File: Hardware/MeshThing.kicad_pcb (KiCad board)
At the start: 4 copper layers, 19.1 x 24.7 mm, 24 parts, among them IC1 ATMEGA2564/1284/644RFR2, P1 CONN34

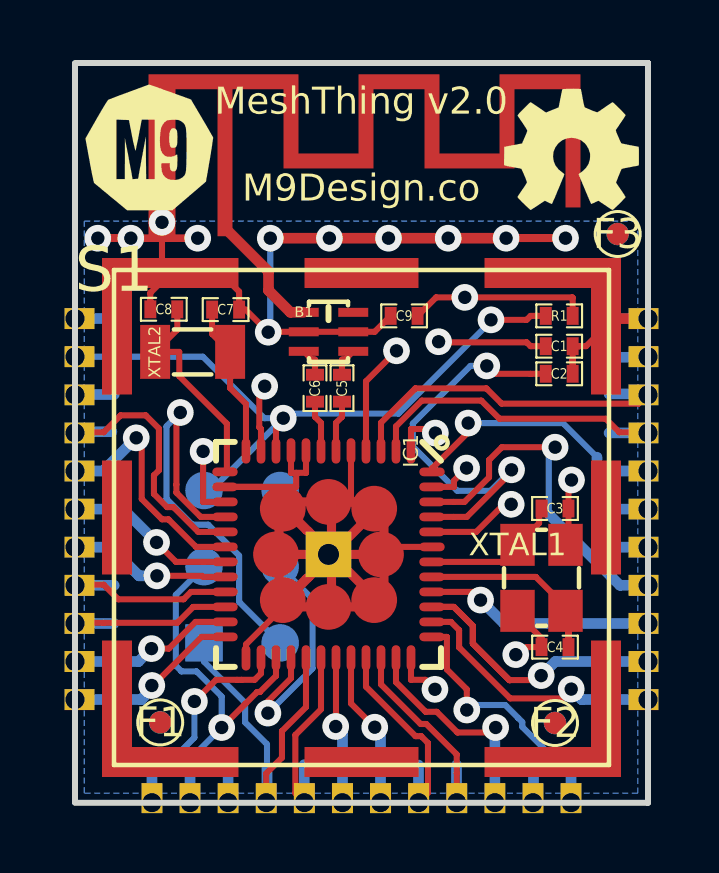
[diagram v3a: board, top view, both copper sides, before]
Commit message: Minor changes, initial positions file for MT.
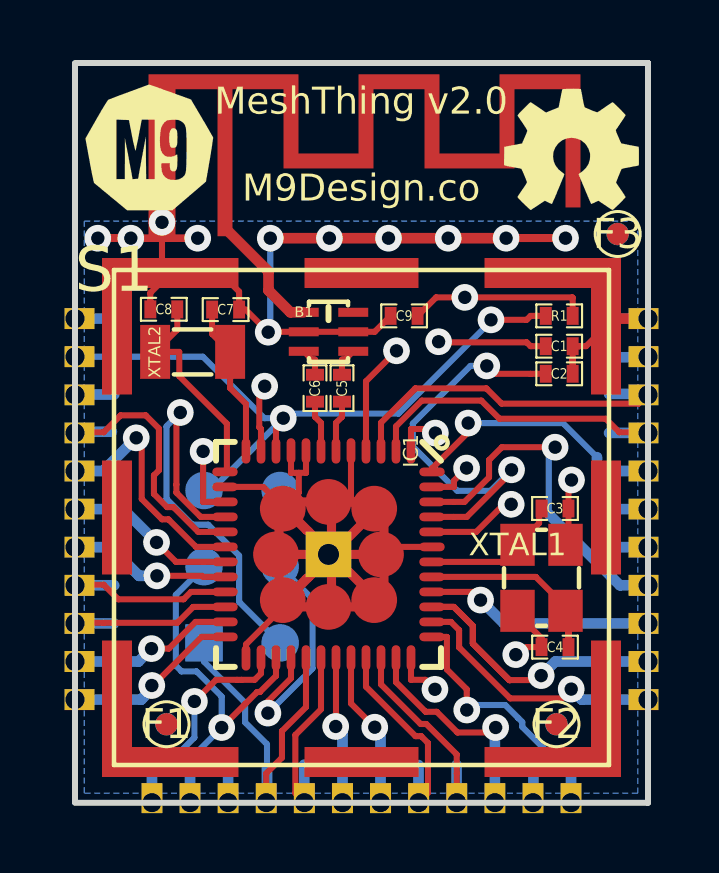
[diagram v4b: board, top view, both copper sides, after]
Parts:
- moved F1 0.22 mm to (143.5, 109.7)
- moved F2 0.06 mm to (156.5, 109.7)
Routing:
- net GND: track 96.3 -> 94.6 mm
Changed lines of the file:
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@@
   )
   (layers
-    (15 F.Cu signal hide)
+    (15 F.Cu signal)
     (2 Inner2.Cu power hide)
     (1 Inner1.Cu signal hide)
@@
     (18 B.Paste user hide)
     (19 F.Paste user hide)
-    (20 B.SilkS user)
+    (20 B.SilkS user hide)
     (21 F.SilkS user hide)
     (22 B.Mask user)
@@
     (aux_axis_origin 150 100)
     (grid_origin 150 100)
-    (visible_elements FFFFCE5B)
+    (visible_elements FFFFCA3B)
     (pcbplotparams
       (layerselection 284983303)
@@
   )
   (module _MT_MC_Pretty:_MT_Fiducial (layer F.Cu)
-    (at 156.45 109.67)
+    (at 156.5 109.71)
+    (attr smd)
     (fp_text reference F2 (at 0 0) (layer F.SilkS)
       (effects (font (size 1 1) (thickness 0.15)))
@@
   )
   (module _MT_MC_Pretty:_MT_Fiducial (layer F.Cu)
-    (at 143.29 109.65)
+    (at 143.5 109.71)
+    (attr smd)
     (fp_text reference F1 (at 0 0) (layer F.SilkS)
       (effects (font (size 1 1) (thickness 0.15)))
@@
   (module _MT_MC_Pretty:16MHz-3.2x2.5mm-TSX-3225 (layer F.Cu)
     (at 156 104.83)
+    (attr smd)
     (fp_text reference XTAL1 (at -0.8 -1.1) (layer F.SilkS)
       (effects (font (size 0.75 0.75) (thickness 0.15)))
@@
   (module _MT_MC_Pretty:_MT_MC_EMIShield-16.5x16.5 (layer F.Cu)
     (at 150 102.82)
+    (attr smd)
     (fp_text reference S1 (at -8.25 -8.25) (layer F.SilkS)
       (effects (font (size 1.5 1.5) (thickness 0.15)))
@@
   (module _MT_MC_Pretty:_MC_TF32D-32768-Crystal (layer F.Cu)
     (at 144.37 97.3)
+    (attr smd)
     (fp_text reference XTAL2 (at -1.26 0 90) (layer F.SilkS)
       (effects (font (size 0.4 0.4) (thickness 0.1)))
@@
   (module _MT_MC_Pretty:_MT_Fiducial (layer F.Cu)
     (at 158.54 93.37)
+    (attr smd)
     (fp_text reference F3 (at 0 0) (layer F.SilkS)
       (effects (font (size 1 1) (thickness 0.15)))
@@
   (segment (start 153.3706 95.41) (end 150.2596 95.41) (width 0.2032) (layer Inner1.Cu) (net 1))
   (segment (start 153.4432 95.4826) (end 153.3706 95.41) (width 0.2032) (layer Inner1.Cu) (net 1))
+  (segment (start 147.91 101.3313) (end 147.91 101.992) (width 0.2032) (layer F.Cu) (net 2))
+  (segment (start 147.91 101.992) (end 147.376 102.526) (width 0.2032) (layer F.Cu) (net 2))
+  (segment (start 147.376 102.526) (end 147.376 102.456) (width 0.2032) (layer F.Cu) (net 2))
+  (segment (start 145.45068 101.8) (end 146.72 101.8) (width 0.2032) (layer F.Cu) (net 2))
+  (segment (start 147.376 102.456) (end 146.72 101.8) (width 0.2032) (layer F.Cu) (net 2))
   (segment (start 150.97042 96.1) (end 150.44042 96.63) (width 0.2032) (layer F.Cu) (net 2))
   (segment (start 150.44042 96.63) (end 149.725 96.63) (width 0.2032) (layer F.Cu) (net 2))
@@
   (segment (start 143.35 93.51) (end 144.54 93.51) (width 0.254) (layer F.Cu) (net 2))
   (via (at 144.54 93.51) (size 0.889) (layers F.Cu B.Cu) (net 2))
-  (segment (start 145.45068 101.8) (end 147.11 101.8) (width 0.2032) (layer F.Cu) (net 2))
-  (segment (start 147.376 102.066) (end 147.376 102.526) (width 0.2032) (layer F.Cu) (net 2))
-  (segment (start 147.11 101.8) (end 147.376 102.066) (width 0.2032) (layer F.Cu) (net 2))
   (segment (start 159.525 96.19) (end 158.26 96.19) (width 0.3556) (layer B.Cu) (net 2))
   (segment (start 145.91958 95.89) (end 146.1378 95.89) (width 0.2032) (layer F.Cu) (net 2))
@@
   (segment (start 148.9 102.3) (end 148.5409 102.3) (width 0.3048) (layer F.Cu) (net 2))
   (segment (start 148.5409 102.3) (end 147.702 102.3) (width 0.3048) (layer F.Cu) (net 2))
-  (segment (start 145.4507 101.8) (end 146.1813 101.8) (width 0.2032) (layer F.Cu) (net 2))
   (segment (start 147.702 105.8) (end 148.9 105.8) (width 0.3048) (layer F.Cu) (net 2))
   (segment (start 146.15 107.05) (end 146.15 107.4993) (width 0.2032) (layer F.Cu) (net 2))
@@
   (segment (start 148.15 100.6007) (end 148.15 101.3313) (width 0.2032) (layer F.Cu) (net 2))
   (segment (start 147.65 100.6007) (end 147.65 101.3313) (width 0.2032) (layer F.Cu) (net 2))
-  (segment (start 148.15 101.3313) (end 147.8219 101.3313) (width 0.2032) (layer F.Cu) (net 2))
+  (segment (start 148.15 101.3313) (end 147.91 101.3313) (width 0.2032) (layer F.Cu) (net 2))
+  (segment (start 147.91 101.3313) (end 147.8219 101.3313) (width 0.2032) (layer F.Cu) (net 2))
   (segment (start 147.8219 101.3313) (end 147.65 101.3313) (width 0.2032) (layer F.Cu) (net 2))
-  (segment (start 147.8219 101.8) (end 146.1813 101.8) (width 0.2032) (layer F.Cu) (net 2))
-  (segment (start 147.8219 101.8) (end 147.8219 101.3313) (width 0.2032) (layer F.Cu) (net 2))
   (segment (start 149.65 102.3) (end 149.65 100.6007) (width 0.2032) (layer F.Cu) (net 2))
   (segment (start 150.298 102.3) (end 149.65 102.3) (width 0.3048) (layer F.Cu) (net 2))

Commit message: Removed ICSP pads.
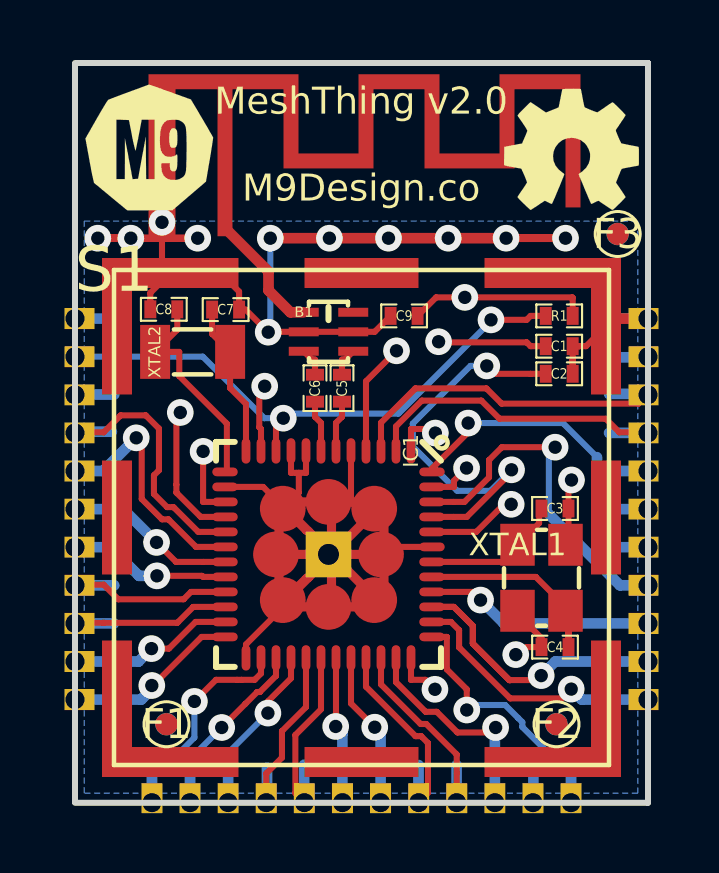
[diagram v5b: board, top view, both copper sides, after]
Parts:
- removed H1: ICSP, _MT_MC_Pretty:_MC_pin_pad_3x2
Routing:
- net +3.3V: track 61.1 -> 51.3 mm
- net SCK: track 15.1 -> 8.41 mm
- net MOSI: track 14.6 -> 8.65 mm
- net MISO: track 11.6 -> 6.53 mm
- net Reset: track 22.9 -> 19.3 mm
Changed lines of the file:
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@@
 (kicad_pcb (version 3) (host pcbnew "(2013-12-14 BZR 4555)-product")
   (general
-    (links 85)
+    (links 79)
     (no_connects 0)
     (area 140.349999 87.569999 159.650001 112.430001)
     (thickness 1.6)
     (drawings 8)
-    (tracks 588)
+    (tracks 565)
     (zones 0)
-    (modules 24)
+    (modules 23)
     (nets 47)
   )
@@
     (aux_axis_origin 150 100)
     (grid_origin 150 100)
-    (visible_elements FFFFCA3B)
+    (visible_elements FFFF4E3B)
     (pcbplotparams
       (layerselection 284983303)
@@
       (xy 1.46558 -0.05842) (xy 1.56718 -0.06858) (xy 1.57988 -0.05842) (xy 1.57988 -0.05842)) (layer B.SilkS) (width 0.00254))
   )
-  (module _MT_MC_Pretty:_MC_pin_pad_3x2 (layer B.Cu)
-    (at 146.02 104.46 90)
-    (descr "Double rangee de contacts 2 x 4 pins")
-    (tags CONN)
-    (fp_text reference H1 (at 0 3.81 90) (layer B.SilkS) hide
-      (effects (font (size 1.016 1.016) (thickness 0.2032)) (justify mirror))
-    )
-    (fp_text value ICSP (at 0 -3.81 90) (layer B.SilkS) hide
-      (effects (font (size 1.016 1.016) (thickness 0.2032)) (justify mirror))
-    )
-    (fp_text user ICSP (at -4.6 0 360) (layer B.SilkS)
-      (effects (font (size 0.5 0.5) (thickness 0.125)) (justify mirror))
-    )
-    (fp_line (start -3.81 2.52) (end -3.81 -1.74) (layer B.SilkS) (width 0.2032))
-    (fp_line (start 3.81 -2.54) (end -3 -2.55) (layer B.SilkS) (width 0.2032))
-    (fp_line (start -3.01 -2.54) (end -3.81 -1.74) (layer B.SilkS) (width 0.2032))
-    (fp_circle (center -3.79 -2.474) (end -4.04 -2.474) (layer B.SilkS) (width 0.254))
-    (fp_line (start -3.81 2.54) (end 3.81 2.54) (layer B.SilkS) (width 0.2032))
-    (fp_line (start 3.81 2.54) (end 3.81 -2.54) (layer B.SilkS) (width 0.2032))
-    (pad 1 smd rect (at -2.54 -1.27 90) (size 1.25 1.25) (layers B.Cu B.Mask)
-      (net 3 MISO))
-    (pad 2 smd circle (at -2.54 1.27 90) (size 1.25 1.25) (layers B.Cu B.Mask)
-      (net 1 +3.3V))
-    (pad 3 smd circle (at 0 -1.27 90) (size 1.25 1.25) (layers B.Cu B.Mask)
-      (net 42 SCK))
-    (pad 4 smd circle (at 0 1.27 90) (size 1.25 1.25) (layers B.Cu B.Mask)
-      (net 4 MOSI))
-    (pad 5 smd circle (at 2.54 -1.27 90) (size 1.25 1.25) (layers B.Cu B.Mask)
-      (net 41 Reset))
-    (pad 6 smd circle (at 2.54 1.27 90) (size 1.25 1.25) (layers B.Cu B.Mask)
-      (net 2 GND))
-    (model pin_array/pins_array_3x2.wrl
-      (at (xyz 0 0 0))
-      (scale (xyz 1 1 1))
-      (rotate (xyz 0 0 0))
-    )
-  )
   (module _MT_OHW_LOGO:LOGO (layer F.Cu)
     (at 157 90.55)
@@
   (segment (start 153.4432 95.4826) (end 152.48698 95.4826) (width 0.2032) (layer F.Cu) (net 1))
   (segment (start 152.48698 95.4826) (end 151.86958 96.1) (width 0.2032) (layer F.Cu) (net 1))
-  (segment (start 147.29 107) (end 145.92 105.63) (width 0.2032) (layer B.Cu) (net 1))
-  (segment (start 143.5 99.78) (end 143.96 99.32) (width 0.2032) (layer B.Cu) (net 1))
-  (segment (start 143.5 102.2) (end 143.5 99.78) (width 0.2032) (layer B.Cu) (net 1))
-  (segment (start 144.36 103.06) (end 143.5 102.2) (width 0.2032) (layer B.Cu) (net 1))
-  (segment (start 144.89 103.06) (end 144.36 103.06) (width 0.2032) (layer B.Cu) (net 1))
-  (segment (start 145.92 104.09) (end 144.89 103.06) (width 0.2032) (layer B.Cu) (net 1))
-  (segment (start 145.92 105.63) (end 145.92 104.09) (width 0.2032) (layer B.Cu) (net 1))
   (segment (start 143.96 99.32) (end 143.96 101.8548) (width 0.2032) (layer Inner1.Cu) (net 1))
   (segment (start 143.96 101.8548) (end 144.4856 102.3804) (width 0.2032) (layer Inner1.Cu) (net 1))
@@
   (segment (start 142.9604 95.6077) (end 142.9604 95.88) (width 0.2032) (layer F.Cu) (net 2))
   (segment (start 142.96 95.6073) (end 142.9604 95.6077) (width 0.2032) (layer F.Cu) (net 2))
-  (segment (start 144.75 107) (end 144.75 107.62526) (width 0.2032) (layer B.Cu) (net 3))
-  (segment (start 146.12 108.99526) (end 146.12 109.65) (width 0.2032) (layer B.Cu) (net 3))
-  (segment (start 144.75 107.62526) (end 146.12 108.99526) (width 0.2032) (layer B.Cu) (net 3))
-  (segment (start 146.85 111.16) (end 146.85 110.38) (width 0.2032) (layer B.Cu) (net 3))
+  (segment (start 146.825 112.325) (end 146.85 112.3) (width 0.3556) (layer B.Cu) (net 3))
   (segment (start 146.85 112.3) (end 146.85 111.16) (width 0.3556) (layer B.Cu) (net 3))
-  (segment (start 146.825 112.325) (end 146.85 112.3) (width 0.3556) (layer B.Cu) (net 3))
-  (segment (start 146.85 110.38) (end 146.12 109.65) (width 0.2032) (layer B.Cu) (net 3))
   (segment (start 146.825 112.305) (end 146.825 111.3499) (width 0.2032) (layer F.Cu) (net 3))
   (segment (start 148.15 107.4993) (end 148.15 108.2299) (width 0.2032) (layer F.Cu) (net 3))
@@
   (segment (start 148.15 109.1392) (end 147.3488 109.9404) (width 0.2032) (layer F.Cu) (net 3))
   (segment (start 148.15 108.2299) (end 148.15 109.1392) (width 0.2032) (layer F.Cu) (net 3))
-  (segment (start 147.29 104.46) (end 148.37 105.54) (width 0.2032) (layer B.Cu) (net 4))
-  (segment (start 148.37 107.85) (end 146.88 109.34) (width 0.2032) (layer B.Cu) (net 4))
-  (segment (start 148.37 105.54) (end 148.37 107.85) (width 0.2032) (layer B.Cu) (net 4))
-  (segment (start 145.555 112.325) (end 145.555 110.665) (width 0.2032) (layer Inner1.Cu) (net 4))
+  (segment (start 145.555 112.325) (end 145.555 110.665) (width 0.2032) (layer B.Cu) (net 4))
+  (segment (start 145.555 110.665) (end 146.88 109.34) (width 0.2032) (layer B.Cu) (net 4))
   (segment (start 146.88 108.95) (end 147.65 108.18) (width 0.2032) (layer F.Cu) (net 4))
   (segment (start 146.88 109.34) (end 146.88 108.95) (width 0.2032) (layer F.Cu) (net 4))
+  (segment (start 147.65 107.4993) (end 147.65 108.18) (width 0.2032) (layer F.Cu) (net 4))
   (via (at 146.88 109.34) (size 0.889) (layers F.Cu B.Cu) (net 4))
-  (segment (start 145.555 110.665) (end 146.88 109.34) (width 0.2032) (layer Inner1.Cu) (net 4))
   (segment (start 145.555 111.3392) (end 145.555 112.325) (width 0.3556) (layer B.Cu) (net 4))
   (segment (start 145.555 111.3392) (end 145.555 112.325) (width 0.2032) (layer B.Cu) (net 4))
   (segment (start 145.555 111.3392) (end 145.555 112.325) (width 0.2032) (layer B.Cu) (net 4))
-  (segment (start 147.65 107.4993) (end 147.65 108.18) (width 0.2032) (layer F.Cu) (net 4))
   (segment (start 148.075 95.98) (end 147.63 95.98) (width 0.3556) (layer F.Cu) (net 5))
   (segment (start 146.9 95.25) (end 146.9 94.62) (width 0.3556) (layer F.Cu) (net 5))
@@
   (segment (start 143.8167 104.3) (end 143.1673 103.6506) (width 0.2032) (layer F.Cu) (net 40))
   (segment (start 144.7201 104.3) (end 143.8167 104.3) (width 0.2032) (layer F.Cu) (net 40))
-  (segment (start 144.75 101.92) (end 144.9826 101.92) (width 0.2032) (layer B.Cu) (net 41))
-  (segment (start 144.9826 101.92) (end 147.3926 99.51) (width 0.2032) (layer B.Cu) (net 41))
   (segment (start 147.3926 99.51) (end 146.76 99.51) (width 0.2032) (layer B.Cu) (net 41))
   (segment (start 144.71 97.46) (end 140.45 97.46) (width 0.2032) (layer B.Cu) (net 41))
@@
   (segment (start 151.2338 99.3568) (end 154.3169 96.2737) (width 0.2032) (layer B.Cu) (net 41))
   (segment (start 147.3926 99.3568) (end 151.2338 99.3568) (width 0.2032) (layer B.Cu) (net 41))
-  (segment (start 145.34 109.82) (end 145.34 108.79) (width 0.2032) (layer B.Cu) (net 42))
-  (segment (start 143.81 105.4) (end 144.75 104.46) (width 0.2032) (layer B.Cu) (net 42))
-  (segment (start 143.81 107.76) (end 143.81 105.4) (width 0.2032) (layer B.Cu) (net 42))
-  (segment (start 144 107.95) (end 143.81 107.76) (width 0.2032) (layer B.Cu) (net 42))
-  (segment (start 144.5 107.95) (end 144 107.95) (width 0.2032) (layer B.Cu) (net 42))
-  (segment (start 145.34 108.79) (end 144.5 107.95) (width 0.2032) (layer B.Cu) (net 42))
+  (segment (start 144.285 110.875) (end 145.34 109.82) (width 0.2032) (layer B.Cu) (net 42))
+  (segment (start 144.285 112.325) (end 144.285 110.875) (width 0.2032) (layer B.Cu) (net 42))
   (segment (start 146.613598 108.636402) (end 146.523598 108.636402) (width 0.2032) (layer F.Cu) (net 42))
   (segment (start 146.523598 108.636402) (end 146.13 109.03) (width 0.2032) (layer F.Cu) (net 42))
-  (segment (start 144.285 112.325) (end 144.285 110.875) (width 0.2032) (layer B.Cu) (net 42))
   (segment (start 145.34 109.82) (end 146.13 109.03) (width 0.2032) (layer F.Cu) (net 42))
   (via (at 145.34 109.82) (size 0.889) (layers F.Cu B.Cu) (net 42))
-  (segment (start 144.285 110.875) (end 145.34 109.82) (width 0.2032) (layer B.Cu) (net 42))
   (segment (start 147.15 108.1) (end 147.15 107.49932) (width 0.2032) (layer F.Cu) (net 42))
   (segment (start 146.613598 108.636402) (end 147.15 108.1) (width 0.2032) (layer F.Cu) (net 42))

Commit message: Minor silks & logo work.
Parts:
- moved PrettyLady 13.3 mm to (143.8, 95.0)
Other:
- board text added: "Open Hardware"
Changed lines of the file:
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@@
     (links 79)
     (no_connects 0)
-    (area 140.349999 87.569999 159.650001 112.430001)
+    (area 136.013186 85.2768 169.635341 113.0282)
     (thickness 1.6)
-    (drawings 8)
+    (drawings 9)
     (tracks 565)
     (zones 0)
@@
     (18 B.Paste user hide)
     (19 F.Paste user hide)
-    (20 B.SilkS user hide)
-    (21 F.SilkS user hide)
+    (20 B.SilkS user)
+    (21 F.SilkS user)
     (22 B.Mask user)
     (23 F.Mask user)
@@
     (aux_axis_origin 150 100)
     (grid_origin 150 100)
-    (visible_elements FFFF4E3B)
+    (visible_elements FFFFCE3B)
     (pcbplotparams
       (layerselection 284983303)
@@
   )
   (module _MT_MC_Pretty:_MC_LOGO-PrettyLady (layer B.Cu)
-    (at 150.37 106.56)
+    (at 143.75 95)
     (fp_text reference PrettyLady (at 0 -3.302) (layer B.SilkS) hide
       (effects (font (thickness 0.3048)) (justify mirror))
@@
       (net 2 GND))
   )
-  (gr_text "Design    by \nRobert Powers" (at 158.2 97.81) (layer B.SilkS)
-    (effects (font (size 1 1) (thickness 0.25)) (justify left mirror))
+  (gr_text "Open Hardware" (at 152.825 98.5) (layer B.SilkS)
+    (effects (font (size 1 1) (thickness 0.175)) (justify mirror))
+  )
+  (gr_text "Design by \nRobert Powers" (at 150 91) (layer B.SilkS)
+    (effects (font (size 1 1) (thickness 0.25)) (justify mirror))
   )
   (gr_line (start 159.55 87.67) (end 140.45 87.67) (angle 90) (layer Edge.Cuts) (width 0.2))
@@
   (gr_line (start 140.45 112.33) (end 159.55 112.33) (angle 90) (layer Edge.Cuts) (width 0.2))
   (gr_line (start 140.45 87.7) (end 140.45 112.31) (angle 90) (layer Edge.Cuts) (width 0.2))
-  (gr_text "      Licensed\nTAPR OHL\ntapr.org/OHL" (at 158.2 103.48) (layer B.SilkS)
+  (gr_text "Licensed\nTAPR OHL\ntapr.org/OHL" (at 151.75 101.5) (layer B.SilkS)
     (effects (font (size 0.8 0.8) (thickness 0.2)) (justify left mirror))
   )
@@
     (effects (font (size 0.9 0.9) (thickness 0.225)))
   )
-  (gr_text "© M9Design.co 2013\n" (at 158.25 94.65) (layer B.SilkS)
-    (effects (font (size 1 1) (thickness 0.25)) (justify left mirror))
+  (gr_text "© M9Design.co 2013\n" (at 150 88.8) (layer B.SilkS)
+    (effects (font (size 1 1) (thickness 0.25)) (justify mirror))
   )
   (segment (start 153.4432 95.4826) (end 152.48698 95.4826) (width 0.2032) (layer F.Cu) (net 1))
